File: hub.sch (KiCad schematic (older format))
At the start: 18 parts, among them J1 USB_C_Receptacle_USB2.0, U14 GL850G, X2 ECS-2520MV-120-xx

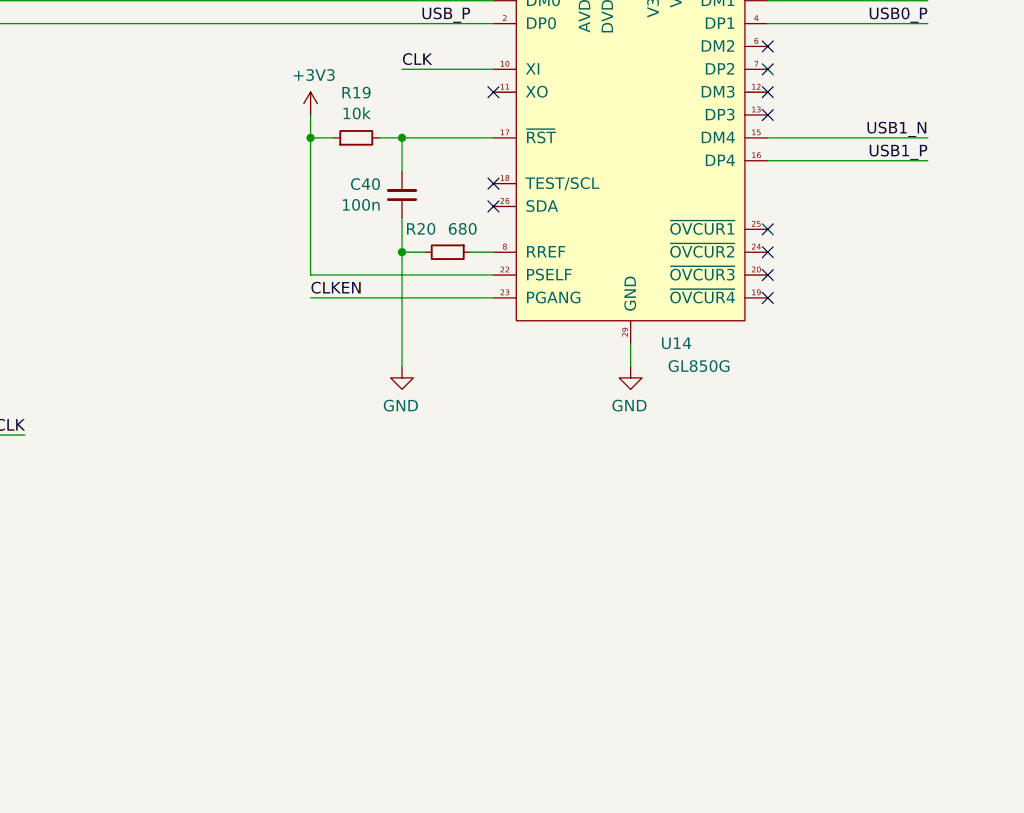
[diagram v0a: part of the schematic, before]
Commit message: sch, pcb: Add I²C EEPROM for USB hub
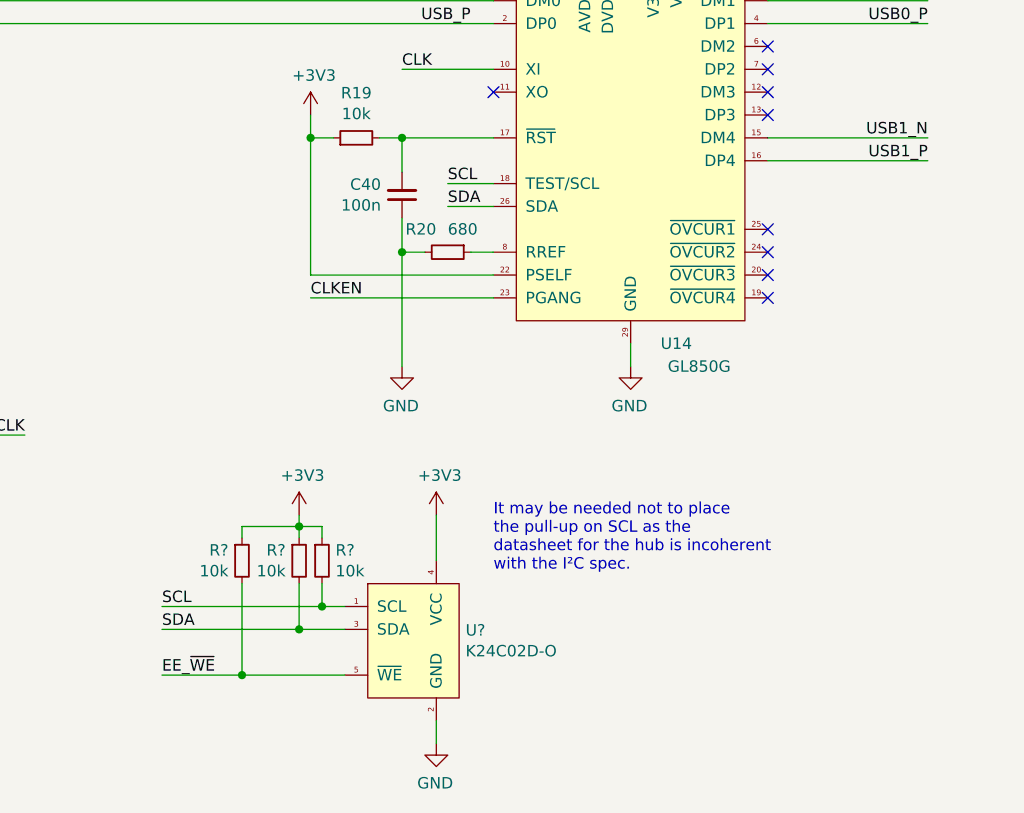
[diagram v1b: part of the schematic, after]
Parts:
- added R? (x3): 10k, Resistor_SMD:R_0603_1608Metric, symbol Device:R_Small
- added U?: K24C02D-O, Package_TO_SOT_SMD:SOT-23-5, symbol antboard:K24C02D-O
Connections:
- net +3V3: now also R?.1, R?.1, R?.1, U?.4 (VCC)
- net GND: now also U?.2 (GND)
- net SCL: now reaches U14.18 (TEST/SCL)
- net SCL: now also R?.2, U?.1 (SCL)
- net SDA: now reaches U14.26 (SDA)
- net SDA: now also R?.2, U?.3 (SDA)
- new net EE_~WE: R?.2, U?.5 (~WE)
- no-connect marks 13 -> 11
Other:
- note added: "It may be needed not to place\nthe pull-up on SCL as the\ndatasheet for the hub is incoherent\nwith the I²C spec."
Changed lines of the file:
@@
 NoConn ~ 7550 3500
 NoConn ~ 7550 3600
-NoConn ~ 6350 4100
-NoConn ~ 6350 4200
 $Comp
 L Device:R_Small R?
@@
 	-1   0    0    -1
 $EndComp
+$Comp
+L antboard:K24C02D-O U?
+U 1 1 5E1D3F3C
+P 5800 5850
+F 0 "U?" H 6228 5646 50  0000 L CNN
+F 1 "K24C02D-O" H 6228 5555 50  0000 L CNN
+F 2 "Package_TO_SOT_SMD:SOT-23-5" H 5800 5850 50  0001 C CNN
+F 3 "https://datasheet.lcsc.com/szlcsc/1809261012_Hua-Hong-NEC-K24C02_C84964.pdf" H 5800 5850 50  0001 C CNN
+	1    5800 5850
+	1    0    0    -1
+$EndComp
+$Comp
+L power:+3V3 #PWR?
+U 1 1 5E1D5771
+P 6100 5550
+F 0 "#PWR?" H 6100 5400 50  0001 C CNN
+F 1 "+3V3" H 6115 5723 50  0000 C CNN
+F 2 "" H 6100 5550 50  0001 C CNN
+F 3 "" H 6100 5550 50  0001 C CNN
+	1    6100 5550
+	1    0    0    -1
+$EndComp
+Wire Wire Line
+	6100 5550 6100 5750
+Wire Wire Line
+	6100 6450 6100 6550
+$Comp
+L power:GND #PWR?
+U 1 1 5E1D752C
+P 6100 6550
+AR Path="/5DFC2583/5E1D752C" Ref="#PWR?"  Part="1"
+AR Path="/5E157F68/5E1D752C" Ref="#PWR?"  Part="1"
+F 0 "#PWR?" H 6100 6300 50  0001 C CNN
+F 1 "GND" H 6105 6377 50  0000 C CNN
+F 2 "" H 6100 6550 50  0001 C CNN
+F 3 "" H 6100 6550 50  0001 C CNN
+	1    6100 6550
+	-1   0    0    -1
+$EndComp
+Wire Wire Line
+	6350 4100 6150 4100
+Wire Wire Line
+	6150 4200 6350 4200
+Text Label 6150 4100 0    50   ~ 0
+SCL
+Text Label 6150 4200 0    50   ~ 0
+SDA
+Text Label 4900 5950 0    50   ~ 0
+SCL
+Text Label 4900 6050 0    50   ~ 0
+SDA
+$Comp
+L Device:R_Small R?
+U 1 1 5E1E2F1C
+P 5600 5750
+AR Path="/5DF7E971/5E1E2F1C" Ref="R?"  Part="1"
+AR Path="/5DFC2583/5E1E2F1C" Ref="R?"  Part="1"
+AR Path="/5E157F68/5E1E2F1C" Ref="R?"  Part="1"
+F 0 "R?" H 5659 5796 50  0000 L CNN
+F 1 "10k" H 5659 5705 50  0000 L CNN
+F 2 "Resistor_SMD:R_0603_1608Metric" H 5600 5750 50  0001 C CNN
+F 3 "~" H 5600 5750 50  0001 C CNN
+	1    5600 5750
+	1    0    0    -1
+$EndComp
+$Comp
+L power:+3V3 #PWR?
+U 1 1 5E1E2F22
+P 5500 5550
+F 0 "#PWR?" H 5500 5400 50  0001 C CNN
+F 1 "+3V3" H 5515 5723 50  0000 C CNN
+F 2 "" H 5500 5550 50  0001 C CNN
+F 3 "" H 5500 5550 50  0001 C CNN
+	1    5500 5550
+	1    0    0    -1
+$EndComp
+$Comp
+L Device:R_Small R?
+U 1 1 5E1E7739
+P 5500 5750
+AR Path="/5DF7E971/5E1E7739" Ref="R?"  Part="1"
+AR Path="/5DFC2583/5E1E7739" Ref="R?"  Part="1"
+AR Path="/5E157F68/5E1E7739" Ref="R?"  Part="1"
+F 0 "R?" H 5441 5796 50  0000 R CNN
+F 1 "10k" H 5441 5705 50  0000 R CNN
+F 2 "Resistor_SMD:R_0603_1608Metric" H 5500 5750 50  0001 C CNN
+F 3 "~" H 5500 5750 50  0001 C CNN
+	1    5500 5750
+	1    0    0    -1
+$EndComp
+Wire Wire Line
+	5500 5650 5500 5600
+Wire Wire Line
+	5600 5600 5600 5650
+Wire Wire Line
+	5500 5550 5500 5600
+$Comp
+L Device:R_Small R?
+U 1 1 5E1FC098
+P 5250 5750
+AR Path="/5DF7E971/5E1FC098" Ref="R?"  Part="1"
+AR Path="/5DFC2583/5E1FC098" Ref="R?"  Part="1"
+AR Path="/5E157F68/5E1FC098" Ref="R?"  Part="1"
+F 0 "R?" H 5191 5796 50  0000 R CNN
+F 1 "10k" H 5191 5705 50  0000 R CNN
+F 2 "Resistor_SMD:R_0603_1608Metric" H 5250 5750 50  0001 C CNN
+F 3 "~" H 5250 5750 50  0001 C CNN
+	1    5250 5750
+	1    0    0    -1
+$EndComp
+Wire Wire Line
+	5250 5650 5250 5600
+Connection ~ 5500 5600
+Wire Wire Line
+	5700 6250 5250 6250
+Wire Wire Line
+	5250 5850 5250 6250
+Connection ~ 5250 6250
+Wire Wire Line
+	5250 6250 4900 6250
+Wire Wire Line
+	4900 5950 5600 5950
+Wire Wire Line
+	4900 6050 5500 6050
+Wire Wire Line
+	5500 5850 5500 6050
+Connection ~ 5500 6050
+Wire Wire Line
+	5500 6050 5700 6050
+Wire Wire Line
+	5600 5850 5600 5950
+Connection ~ 5600 5950
+Wire Wire Line
+	5600 5950 5700 5950
+Wire Wire Line
+	5500 5600 5600 5600
+Wire Wire Line
+	5250 5600 5500 5600
+Text Label 4900 6250 0    50   ~ 0
+EE_~WE
+Text Notes 6350 5800 0    50   ~ 0
+It may be needed not to place\nthe pull-up on SCL as the\ndatasheet for the hub is incoherent\nwith the I²C spec.
 $EndSCHEMATC

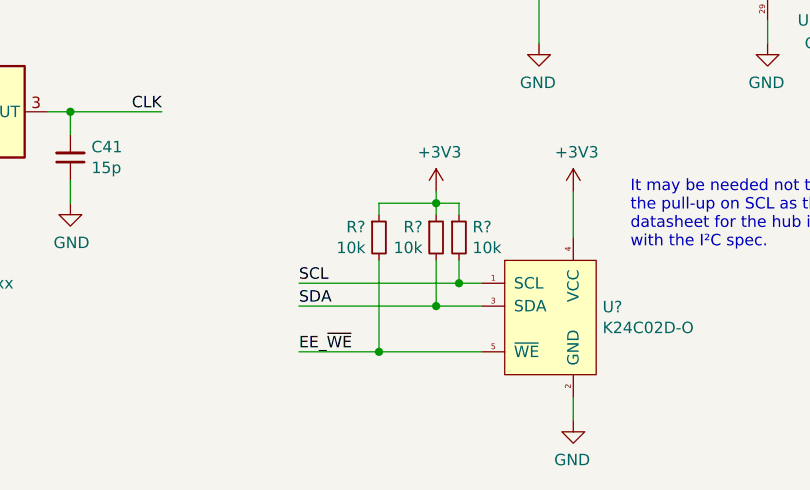
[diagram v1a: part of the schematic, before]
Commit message: sch, pcb: Add header to access EEPROM I²C bus
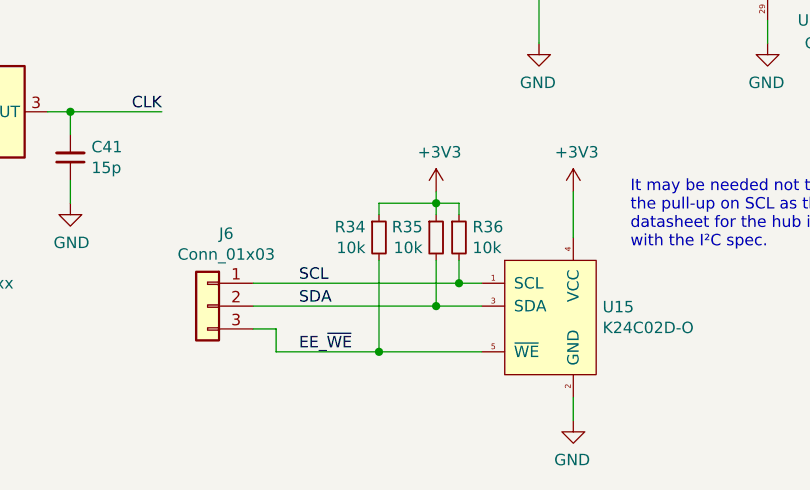
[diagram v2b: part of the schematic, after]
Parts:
- added J6: Conn_01x03, Connector_PinHeader_2.54mm:PinHeader_1x03_P2.54mm_Vertical, symbol Connector_Generic:Conn_01x03
- gave numbers to parts that had none: 4
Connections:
- net EE_~WE: now also J6.3 (Pin_3)
- net SCL: now also J6.1 (Pin_1)
- net SDA: now also J6.2 (Pin_2)
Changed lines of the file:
@@
 $EndComp
 $Comp
-L antboard:K24C02D-O U?
+L antboard:K24C02D-O U15
 U 1 1 5E1D3F3C
 P 5800 5850
-F 0 "U?" H 6228 5646 50  0000 L CNN
+F 0 "U15" H 6228 5646 50  0000 L CNN
 F 1 "K24C02D-O" H 6228 5555 50  0000 L CNN
 F 2 "Package_TO_SOT_SMD:SOT-23-5" H 5800 5850 50  0001 C CNN
@@
 $EndComp
 $Comp
-L power:+3V3 #PWR?
+L power:+3V3 #PWR059
 U 1 1 5E1D5771
 P 6100 5550
-F 0 "#PWR?" H 6100 5400 50  0001 C CNN
+F 0 "#PWR059" H 6100 5400 50  0001 C CNN
 F 1 "+3V3" H 6115 5723 50  0000 C CNN
 F 2 "" H 6100 5550 50  0001 C CNN
@@
 P 6100 6550
 AR Path="/5DFC2583/5E1D752C" Ref="#PWR?"  Part="1"
-AR Path="/5E157F68/5E1D752C" Ref="#PWR?"  Part="1"
-F 0 "#PWR?" H 6100 6300 50  0001 C CNN
+AR Path="/5E157F68/5E1D752C" Ref="#PWR060"  Part="1"
+F 0 "#PWR060" H 6100 6300 50  0001 C CNN
 F 1 "GND" H 6105 6377 50  0000 C CNN
 F 2 "" H 6100 6550 50  0001 C CNN
@@
 AR Path="/5DF7E971/5E1E2F1C" Ref="R?"  Part="1"
 AR Path="/5DFC2583/5E1E2F1C" Ref="R?"  Part="1"
-AR Path="/5E157F68/5E1E2F1C" Ref="R?"  Part="1"
-F 0 "R?" H 5659 5796 50  0000 L CNN
+AR Path="/5E157F68/5E1E2F1C" Ref="R36"  Part="1"
+F 0 "R36" H 5659 5796 50  0000 L CNN
 F 1 "10k" H 5659 5705 50  0000 L CNN
 F 2 "Resistor_SMD:R_0603_1608Metric" H 5600 5750 50  0001 C CNN
@@
 $EndComp
 $Comp
-L power:+3V3 #PWR?
+L power:+3V3 #PWR058
 U 1 1 5E1E2F22
 P 5500 5550
-F 0 "#PWR?" H 5500 5400 50  0001 C CNN
+F 0 "#PWR058" H 5500 5400 50  0001 C CNN
 F 1 "+3V3" H 5515 5723 50  0000 C CNN
 F 2 "" H 5500 5550 50  0001 C CNN
@@
 AR Path="/5DF7E971/5E1E7739" Ref="R?"  Part="1"
 AR Path="/5DFC2583/5E1E7739" Ref="R?"  Part="1"
-AR Path="/5E157F68/5E1E7739" Ref="R?"  Part="1"
-F 0 "R?" H 5441 5796 50  0000 R CNN
+AR Path="/5E157F68/5E1E7739" Ref="R35"  Part="1"
+F 0 "R35" H 5441 5796 50  0000 R CNN
 F 1 "10k" H 5441 5705 50  0000 R CNN
 F 2 "Resistor_SMD:R_0603_1608Metric" H 5500 5750 50  0001 C CNN
@@
 AR Path="/5DF7E971/5E1FC098" Ref="R?"  Part="1"
 AR Path="/5DFC2583/5E1FC098" Ref="R?"  Part="1"
-AR Path="/5E157F68/5E1FC098" Ref="R?"  Part="1"
-F 0 "R?" H 5191 5796 50  0000 R CNN
+AR Path="/5E157F68/5E1FC098" Ref="R34"  Part="1"
+F 0 "R34" H 5191 5796 50  0000 R CNN
 F 1 "10k" H 5191 5705 50  0000 R CNN
 F 2 "Resistor_SMD:R_0603_1608Metric" H 5250 5750 50  0001 C CNN
@@
 	5250 5850 5250 6250
 Connection ~ 5250 6250
-Wire Wire Line
-	5250 6250 4900 6250
-Wire Wire Line
-	4900 5950 5600 5950
-Wire Wire Line
-	4900 6050 5500 6050
 Wire Wire Line
 	5500 5850 5500 6050
@@
 Text Notes 6350 5800 0    50   ~ 0
 It may be needed not to place\nthe pull-up on SCL as the\ndatasheet for the hub is incoherent\nwith the I²C spec.
+$Comp
+L Connector_Generic:Conn_01x03 J6
+U 1 1 5E2516CB
+P 4500 6050
+F 0 "J6" H 4418 6367 50  0000 C CNN
+F 1 "Conn_01x03" H 4418 6276 50  0000 C CNN
+F 2 "Connector_PinHeader_2.54mm:PinHeader_1x03_P2.54mm_Vertical" H 4500 6050 50  0001 C CNN
+F 3 "~" H 4500 6050 50  0001 C CNN
+	1    4500 6050
+	-1   0    0    -1
+$EndComp
+Wire Wire Line
+	4800 6250 4800 6150
+Wire Wire Line
+	4800 6150 4700 6150
+Wire Wire Line
+	4800 6250 5250 6250
+Wire Wire Line
+	4700 6050 5500 6050
+Wire Wire Line
+	4700 5950 5600 5950
 $EndSCHEMATC

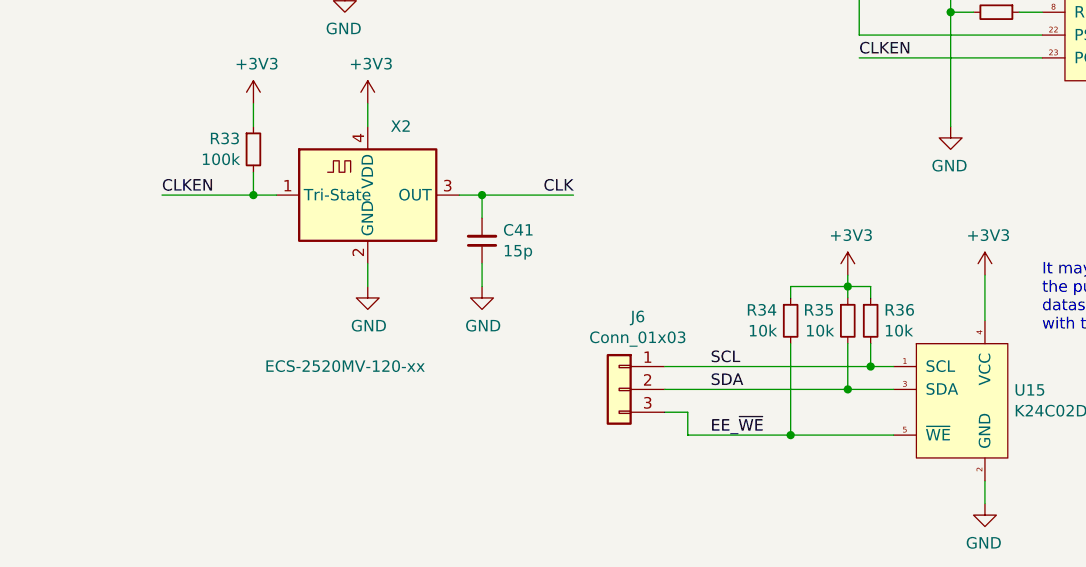
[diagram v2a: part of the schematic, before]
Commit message: sch, pcb: Remove CLKEN and EEPROM SCL pullup
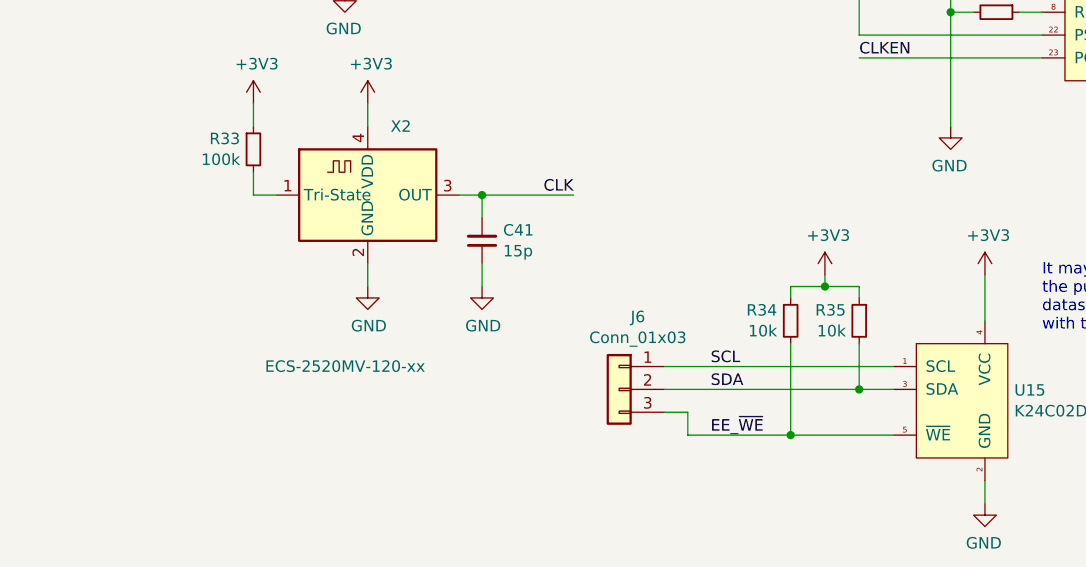
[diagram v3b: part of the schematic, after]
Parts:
- removed R36: 10k, Resistor_SMD:R_0603_1608Metric, symbol Device:R_Small
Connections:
- net CLKEN: no longer R33.2, X2.1 (Tri-State)
- new net: R33.2, X2.1 (Tri-State)
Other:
- moved on the sheet: R35
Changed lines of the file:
@@
 Wire Wire Line
 	3000 5200 2900 5200
-Text Label 2500 5200 0    50   ~ 0
-CLKEN
 $Comp
 L Device:R_Small R?
@@
 Wire Wire Line
 	2900 5100 2900 5200
-Connection ~ 2900 5200
-Wire Wire Line
-	2900 5200 2500 5200
 Wire Wire Line
 	2900 4900 2900 4800
@@
 $Comp
 L Device:R_Small R?
-U 1 1 5E1E2F1C
-P 5600 5750
-AR Path="/5DF7E971/5E1E2F1C" Ref="R?"  Part="1"
-AR Path="/5DFC2583/5E1E2F1C" Ref="R?"  Part="1"
-AR Path="/5E157F68/5E1E2F1C" Ref="R36"  Part="1"
-F 0 "R36" H 5659 5796 50  0000 L CNN
-F 1 "10k" H 5659 5705 50  0000 L CNN
-F 2 "Resistor_SMD:R_0603_1608Metric" H 5600 5750 50  0001 C CNN
-F 3 "~" H 5600 5750 50  0001 C CNN
-	1    5600 5750
-	1    0    0    -1
-$EndComp
-$Comp
-L power:+3V3 #PWR058
-U 1 1 5E1E2F22
-P 5500 5550
-F 0 "#PWR058" H 5500 5400 50  0001 C CNN
-F 1 "+3V3" H 5515 5723 50  0000 C CNN
-F 2 "" H 5500 5550 50  0001 C CNN
-F 3 "" H 5500 5550 50  0001 C CNN
-	1    5500 5550
-	1    0    0    -1
-$EndComp
-$Comp
-L Device:R_Small R?
 U 1 1 5E1E7739
-P 5500 5750
+P 5550 5750
 AR Path="/5DF7E971/5E1E7739" Ref="R?"  Part="1"
 AR Path="/5DFC2583/5E1E7739" Ref="R?"  Part="1"
 AR Path="/5E157F68/5E1E7739" Ref="R35"  Part="1"
-F 0 "R35" H 5441 5796 50  0000 R CNN
-F 1 "10k" H 5441 5705 50  0000 R CNN
-F 2 "Resistor_SMD:R_0603_1608Metric" H 5500 5750 50  0001 C CNN
-F 3 "~" H 5500 5750 50  0001 C CNN
-	1    5500 5750
-	1    0    0    -1
-$EndComp
-Wire Wire Line
-	5500 5650 5500 5600
-Wire Wire Line
-	5600 5600 5600 5650
-Wire Wire Line
-	5500 5550 5500 5600
+F 0 "R35" H 5608 5796 50  0000 L CNN
+F 1 "10k" H 5608 5705 50  0000 L CNN
+F 2 "Resistor_SMD:R_0603_1608Metric" H 5550 5750 50  0001 C CNN
+F 3 "~" H 5550 5750 50  0001 C CNN
+	1    5550 5750
+	-1   0    0    -1
+$EndComp
+Wire Wire Line
+	5550 5650 5550 5600
 $Comp
 L Device:R_Small R?
@@
 Wire Wire Line
 	5250 5650 5250 5600
-Connection ~ 5500 5600
 Wire Wire Line
 	5700 6250 5250 6250
@@
 Connection ~ 5250 6250
 Wire Wire Line
-	5500 5850 5500 6050
-Connection ~ 5500 6050
-Wire Wire Line
-	5500 6050 5700 6050
-Wire Wire Line
-	5600 5850 5600 5950
-Connection ~ 5600 5950
-Wire Wire Line
-	5600 5950 5700 5950
-Wire Wire Line
-	5500 5600 5600 5600
-Wire Wire Line
-	5250 5600 5500 5600
+	5550 5850 5550 6050
+Connection ~ 5550 6050
+Wire Wire Line
+	5550 6050 5700 6050
 Text Label 4900 6250 0    50   ~ 0
 EE_~WE
@@
 	4800 6250 5250 6250
 Wire Wire Line
-	4700 6050 5500 6050
-Wire Wire Line
-	4700 5950 5600 5950
+	4700 6050 5550 6050
+Wire Wire Line
+	4700 5950 5700 5950
+Connection ~ 5400 5600
+Wire Wire Line
+	5250 5600 5400 5600
+Wire Wire Line
+	5400 5600 5550 5600
+Wire Wire Line
+	5400 5550 5400 5600
+$Comp
+L power:+3V3 #PWR058
+U 1 1 5E1E2F22
+P 5400 5550
+F 0 "#PWR058" H 5400 5400 50  0001 C CNN
+F 1 "+3V3" H 5415 5723 50  0000 C CNN
+F 2 "" H 5400 5550 50  0001 C CNN
+F 3 "" H 5400 5550 50  0001 C CNN
+	1    5400 5550
+	1    0    0    -1
+$EndComp
 $EndSCHEMATC
